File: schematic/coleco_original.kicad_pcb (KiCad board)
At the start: 2 copper layers, 168.4 x 318 mm, 220 parts, among them J0 Conn_01x04, J1 Cartridge Port, J2 Expansion Port, J4A1 Conn_01x08, J4B1 Conn_01x08, J5 DB9_Male, J6 DB9_Male, Q2 2N3906, Q3 2N3906, Q4 2N3904, Q5 2N3904, Q6 2N3906, U1 Z80CPU, U10 MK4116P, U11 MK4116P, U12 MK4116P, U13 MK4116P, U14 MK4116P, U15 MK4116P, U16 MK4116P, U17 MK4116P, U18 74LS541, U19 74LS541, U2 27C256, U20 SN76489AN, U22 74LS04, U23 4066, U24 74LS00, U3 SCM2114AL, U4 SCM2114AL, U5 74LS138, U6 74LS138, U7 74LS05, U8 74LS74, U9 TMS9928A, Y1 7.159090Mhz

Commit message: did a small amount of pcb work, also finished component directions for the main board. RF pcb is still a mess and needs a second pass.
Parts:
- moved RF_JP1 15.2 mm to (113.0, 309.0), turned to -90 degrees
- moved R10 10.2 mm to (188.5, 218.3), turned to 90 degrees
- moved R14 10.2 mm to (109.2, 219.1), turned to 180 degrees
- moved R15 10.2 mm to (180.6, 199.3), turned to -90 degrees
- moved R22 10.2 mm to (96.5, 129.9), turned to -90 degrees
- moved R69 10.2 mm to (96.5, 105.8), turned to -90 degrees
- moved R23 9.92 mm to (103.6, 148.2), turned to -90 degrees
- moved R24 9.91 mm to (95.5, 147.7), turned to -90 degrees
- moved R62 9.91 mm to (189.0, 160.9), turned to -90 degrees
- moved R72 9.91 mm to (92.7, 107.1), turned to -90 degrees
- moved R13 9.91 mm to (197.1, 151.0), turned to 0 degrees
- moved R71 9.66 mm to (108.5, 146.2), turned to -90 degrees
- moved R12 9.66 mm to (105.2, 214.0), turned to 180 degrees
- moved R61 9.65 mm to (213.4, 128.9), turned to -90 degrees
- moved R64 9.40 mm to (194.1, 104.8), turned to 180 degrees
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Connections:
- RF_C12 pad 1: Net-(RF_C12-Pad1) -> Net-(RF_SW1-Pad1)
- RF_SW1 pad 1: Net-(RF_C6-Pad1) -> Net-(RF_SW1-Pad1)
- RF_SW1 pad 2: Net-(RF_C12-Pad1) -> Net-(RF_C6-Pad1)
- RF_VL1 pad 1: Net-(RF_C1-Pad1) -> Net-(RF_D2-Pad1)
- RF_VL1 pad 3: Net-(RF_D2-Pad1) -> Net-(RF_C1-Pad1)
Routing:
- net Net-(RF_C1-Pad1): track 0.00 -> 144.0 mm
- net Net-(RF_C6-Pad1): track 0.00 -> 87.2 mm
- net VDDF: track 0.00 -> 85.2 mm
- net Net-(RF_C12-Pad2): track 0.00 -> 81.0 mm
- net Net-(RF_D2-Pad1): track 0.00 -> 56.8 mm
- net /rf_mod/sub_rf_mod/5: track 0.00 -> 56.8 mm
- net /rf_mod/sub_rf_mod/6: track 0.00 -> 41.0 mm
- net Net-(RF_SW1-Pad1): track 0.00 -> 40.2 mm
- net /rf_mod/sub_rf_mod/7: track 0.00 -> 31.2 mm
- net Net-(RF_C7-Pad2): track 0.00 -> 29.5 mm
- net /rf_mod/sub_rf_mod/2: track 0.00 -> 26.2 mm
- net /rf_mod/sub_rf_mod/3: track 0.00 -> 25.4 mm
- net Net-(RF_L2-Pad1): track 0.00 -> 21.8 mm
- net Net-(RF_C10-Pad2): track 0.00 -> 16.4 mm
- net Net-(RF_C5-Pad1): track 0.00 -> 15.7 mm
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- added copper zone on B.Cu, net GNDD

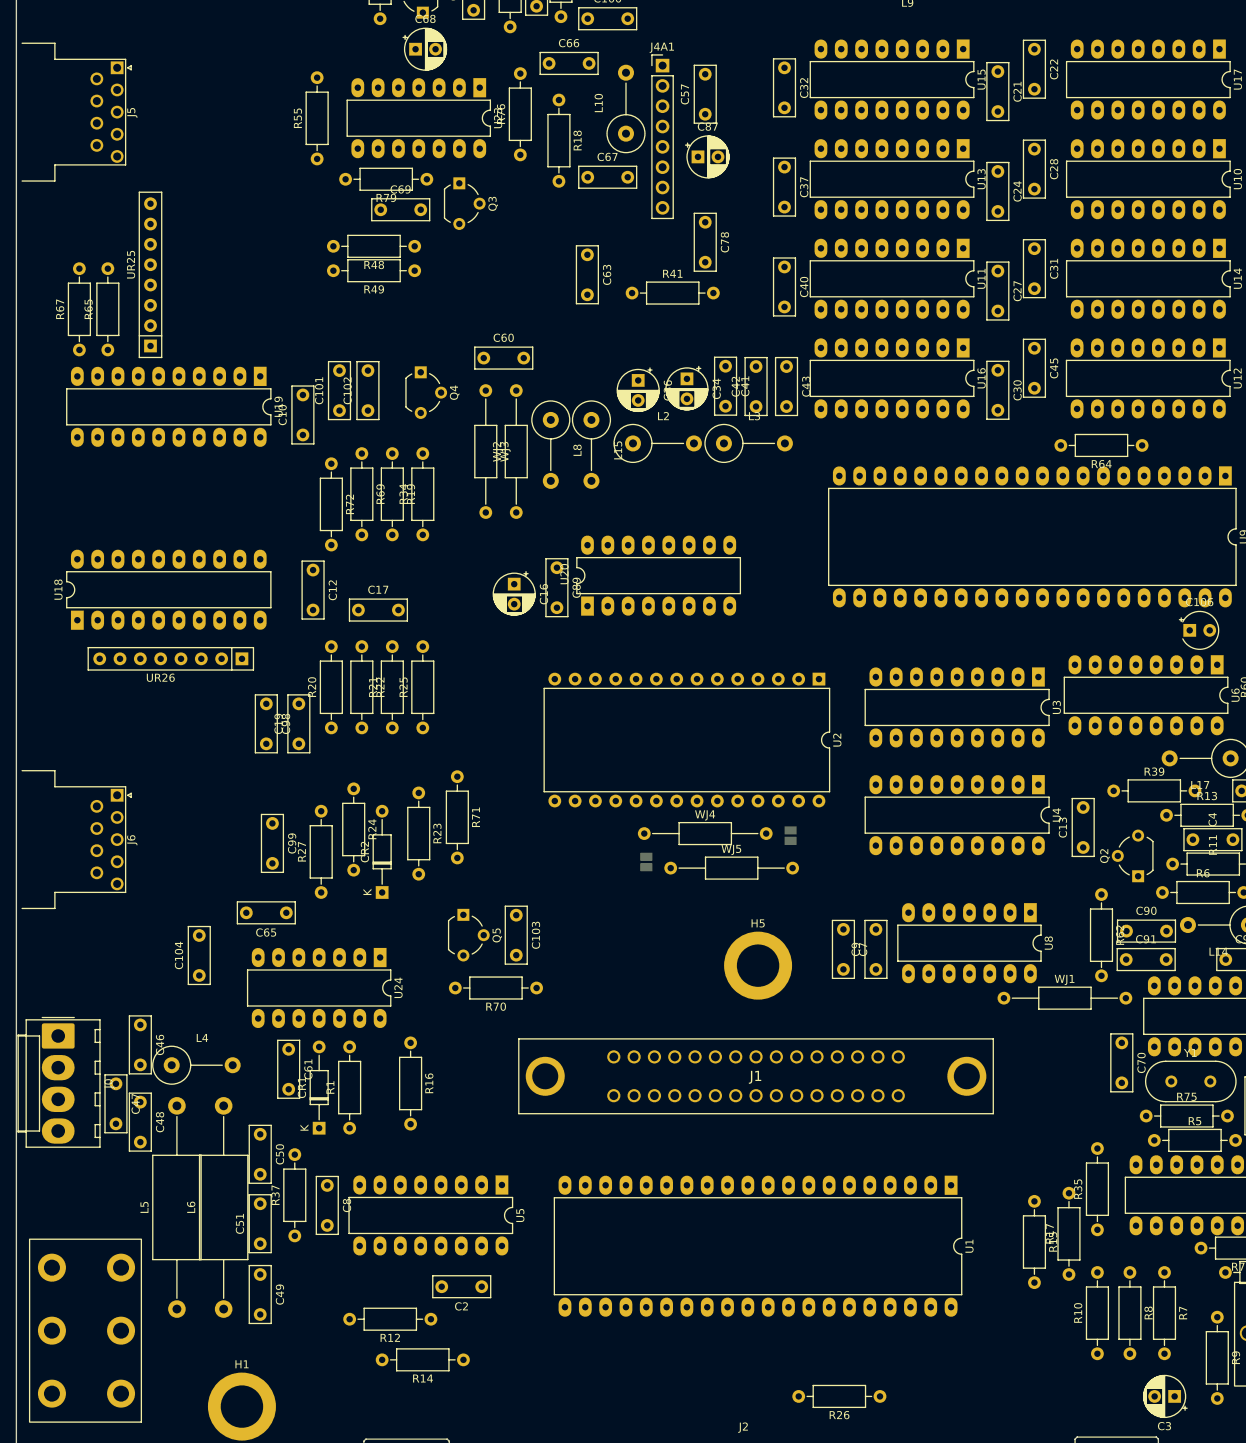
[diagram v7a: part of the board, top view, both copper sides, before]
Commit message: added controller traces and some around it.
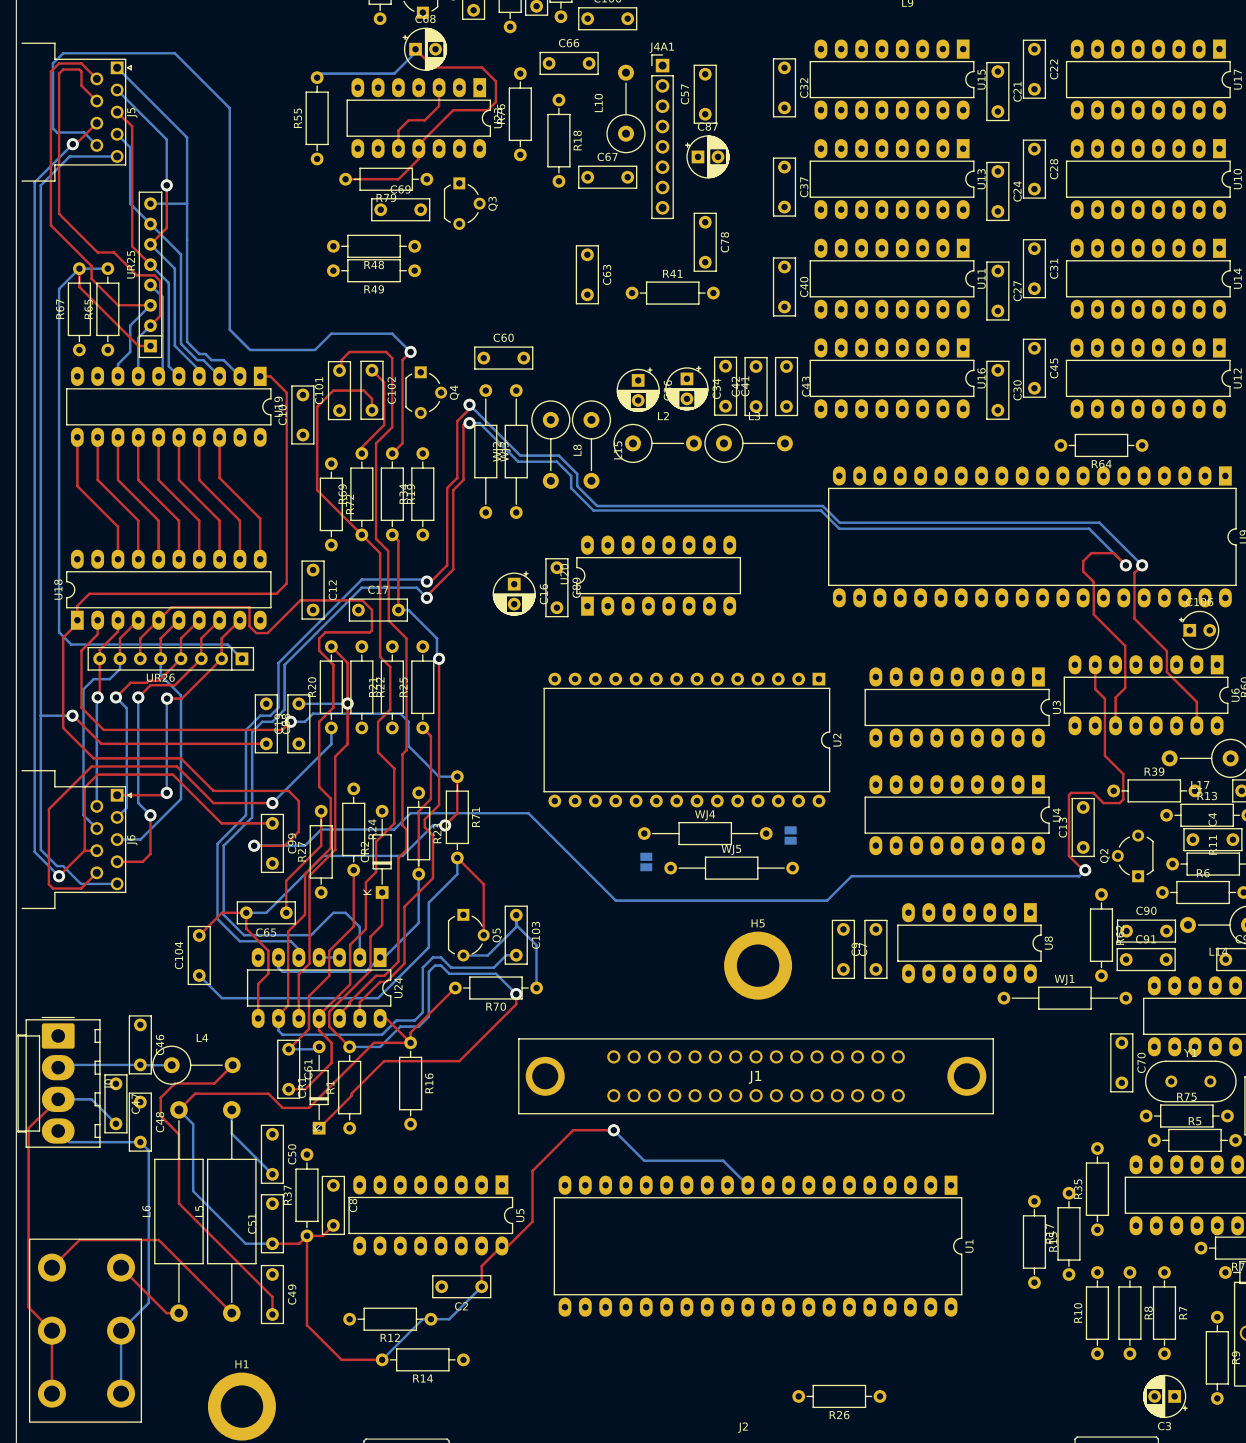
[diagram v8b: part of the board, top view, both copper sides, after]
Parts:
- moved R69 10.2 mm to (96.5, 116.0), turned to 90 degrees
- moved L5 6.88 mm to (80.3, 213.2)
- moved L6 5.61 mm to (73.7, 213.2)
- moved C102 5.07 mm to (97.8, 95.4), turned to -90 degrees
- moved C49 1.52 mm to (85.3, 208.4)
- moved C50 1.52 mm to (85.3, 190.9)
- moved C51 1.52 mm to (85.3, 204.6)
- moved R37 1.52 mm to (89.7, 203.6)
- moved C8 0.76 mm to (93.0, 197.3)
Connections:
- C104 pad 2: Net-(C104-Pad2) -> Net-(U18-Pad2)
- C65 pad 2: Net-(C104-Pad2) -> Net-(U18-Pad2)
- R71 pad 1: Net-(C104-Pad2) -> Net-(U18-Pad2)
- U18 pad 2: unconnected-(U18-Pad2) -> Net-(U18-Pad2)
- U24 pad 8: Net-(C104-Pad2) -> Net-(U18-Pad2)
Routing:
- net /controller/~{CTRL_READ}: track 0.00 -> 262.7 mm, vias 0 -> 2
- net /controller/~{CTRL_EN_1}: track 0.00 -> 225.5 mm, vias 0 -> 3
- net /controller/~{CTRL_EN_2}: track 0.00 -> 213.2 mm, vias 0 -> 3
- net +5V: track 0.00 -> 168.3 mm, vias 0 -> 1
- net Net-(C103-Pad2): track 0.00 -> 139.8 mm
- net Net-(C99-Pad1): track 0.00 -> 139.4 mm, vias 0 -> 2
- net Net-(C98-Pad2): track 0.00 -> 135.1 mm, vias 0 -> 1
- net Net-(U18-Pad2): track 0.00 -> 123.8 mm, vias 0 -> 2
- net Net-(C101-Pad2): track 0.00 -> 110.2 mm
- net Net-(C102-Pad2): track 0.00 -> 108.1 mm
- net Net-(J5-Pad9): track 0.00 -> 106.7 mm, vias 0 -> 1
- net Net-(R65-Pad2): track 0.00 -> 88.5 mm
- net /clock_reset_misc_logic/INT: track 0.00 -> 85.3 mm, vias 0 -> 1
- net Net-(C17-Pad2): track 0.00 -> 69.0 mm, vias 0 -> 1
- net Net-(J6-Pad9): track 0.00 -> 60.9 mm, vias 0 -> 1
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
